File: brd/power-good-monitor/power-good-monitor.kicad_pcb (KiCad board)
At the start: 2 copper layers, 50 x 50 mm, 27 parts, among them J1 POWER IN, J2 CASC IN, J3 POWER GOOD, J4 CASC OUT, Q1 DMP3028LK3-13, Q2 2N7002, Q3 DMP3028LK3-13, U1 TPS3701

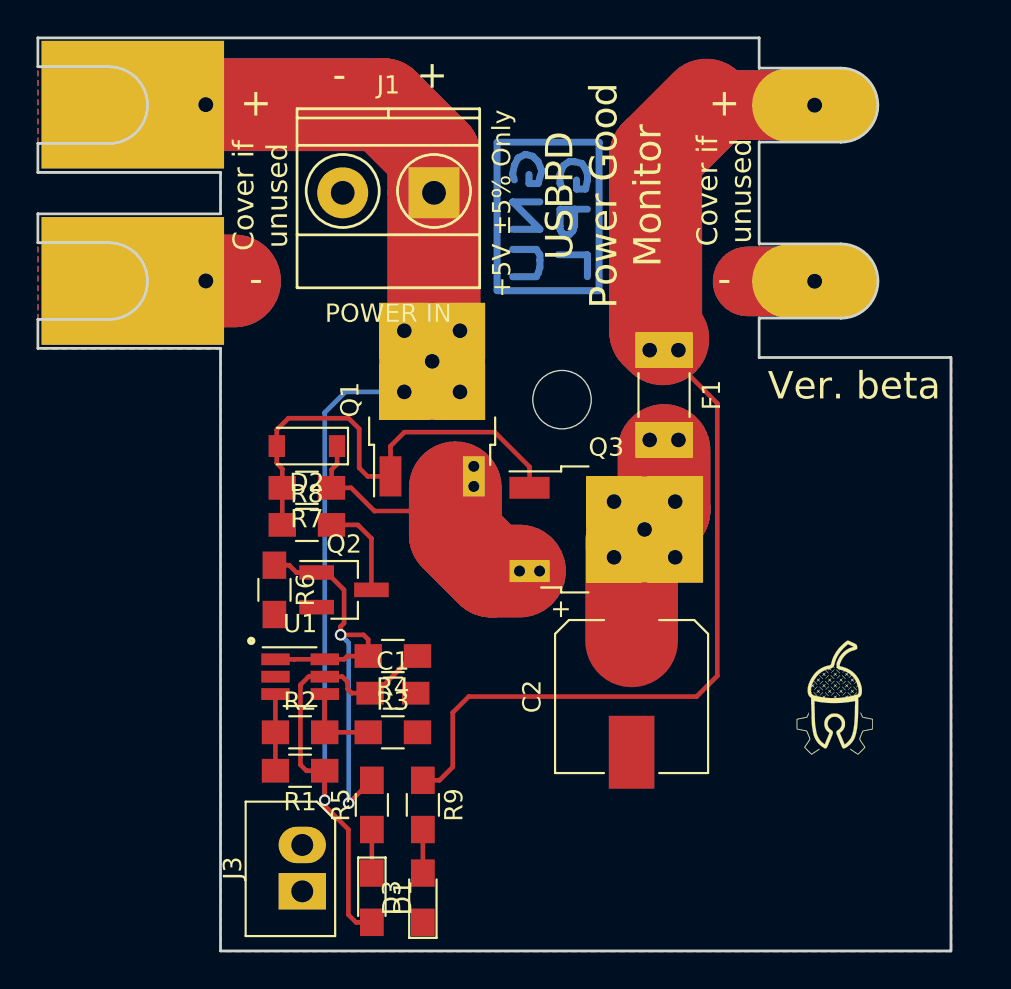
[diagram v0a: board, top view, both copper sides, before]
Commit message: añadidos nuevos componentes para salida de drenador abierto, editada serigrafia
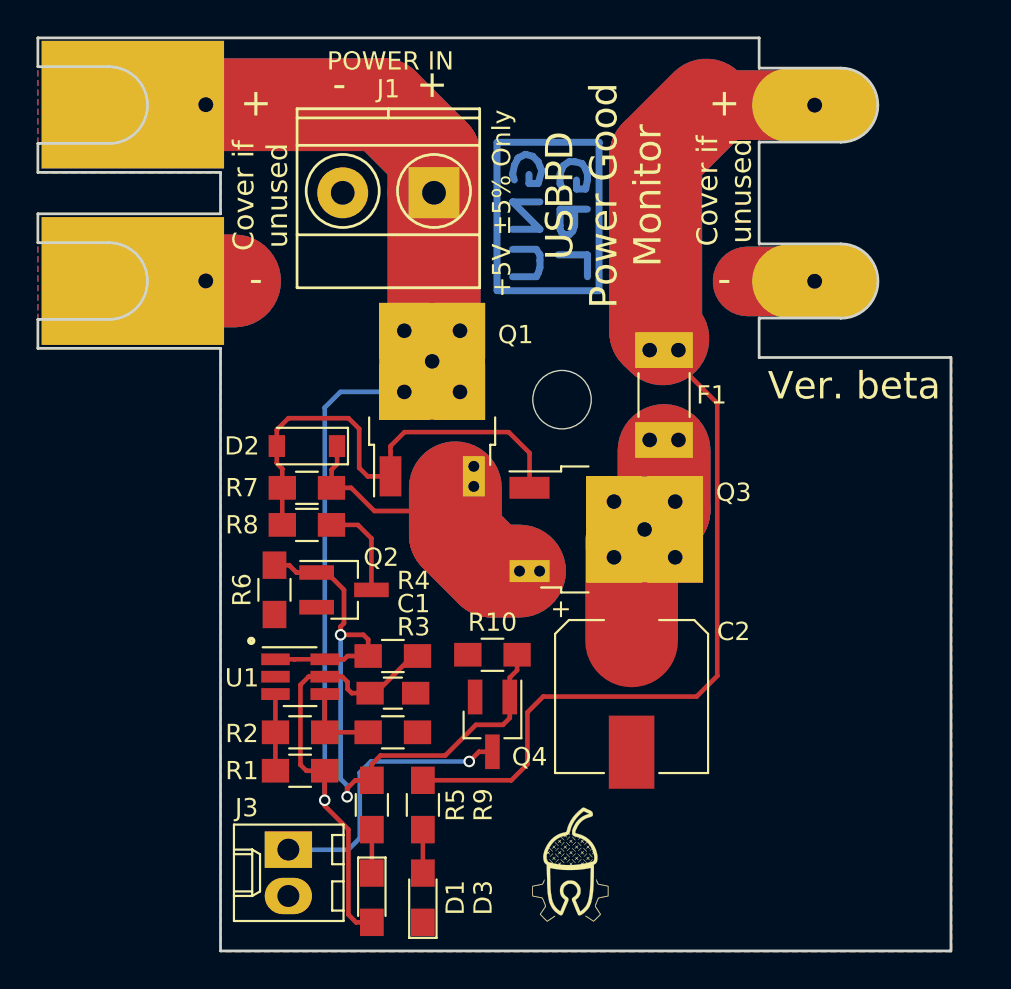
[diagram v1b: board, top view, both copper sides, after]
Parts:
- added Q4: 2N7002, TO_SOT_Packages_SMD:SOT-23_Handsoldering, F.Cu at (147.8, 118.6)
- added R10: 100k, Resistors_SMD:R_0805_HandSoldering, F.Cu at (147.8, 114.8)
- J3: footprint Connectors_Molex:Molex_SPOX-5267_22-03-5025_02x2.54mm_Straight -> Connectors_Molex:Molex_KK-6410-02_02x2.54mm_Straight
- Q1, Q3: value DMP3028LK3-13 -> DMP3028
- moved G*** 17.1 mm to (152.4, 126.2)
- moved J3 2.41 mm to (136.7, 125.5), turned to 270 degrees
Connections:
- Q2 pad 1: Net-(J3-Pad1) -> Net-(Q2-Pad1)
- R4 pad 2: Net-(J3-Pad1) -> Net-(Q2-Pad1)
- R5 pad 2: Net-(J3-Pad1) -> Net-(Q2-Pad1)
- R6 pad 1: Net-(J3-Pad1) -> Net-(Q2-Pad1)
- U1 pad 1: Net-(J3-Pad1) -> Net-(Q2-Pad1)
- U1 pad 6: Net-(J3-Pad1) -> Net-(Q2-Pad1)
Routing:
- net Net-(Q2-Pad1): track 0.00 -> 38.8 mm, vias 0 -> 2
- net Net-(J3-Pad1): track 25.9 -> 15.5 mm, vias 2 -> 1
- net Net-(D2-Pad1): track 26.1 -> 28.3 mm
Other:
- board text added: "Power Good Monitor according USB-IF Spec 11.4.2. Voltage between 4.45 to 5.25V"
- board text added: "SN:k698F61A901a_4517"
- board text removed: "Current R3/R4 100mA 226k 500mA 52k3 900mA 28k7 1500mA 16k9 ** No lim See doc"
- board text removed: "SN:k698F61A900e_4417"
